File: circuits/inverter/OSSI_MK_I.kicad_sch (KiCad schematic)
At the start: 0 parts

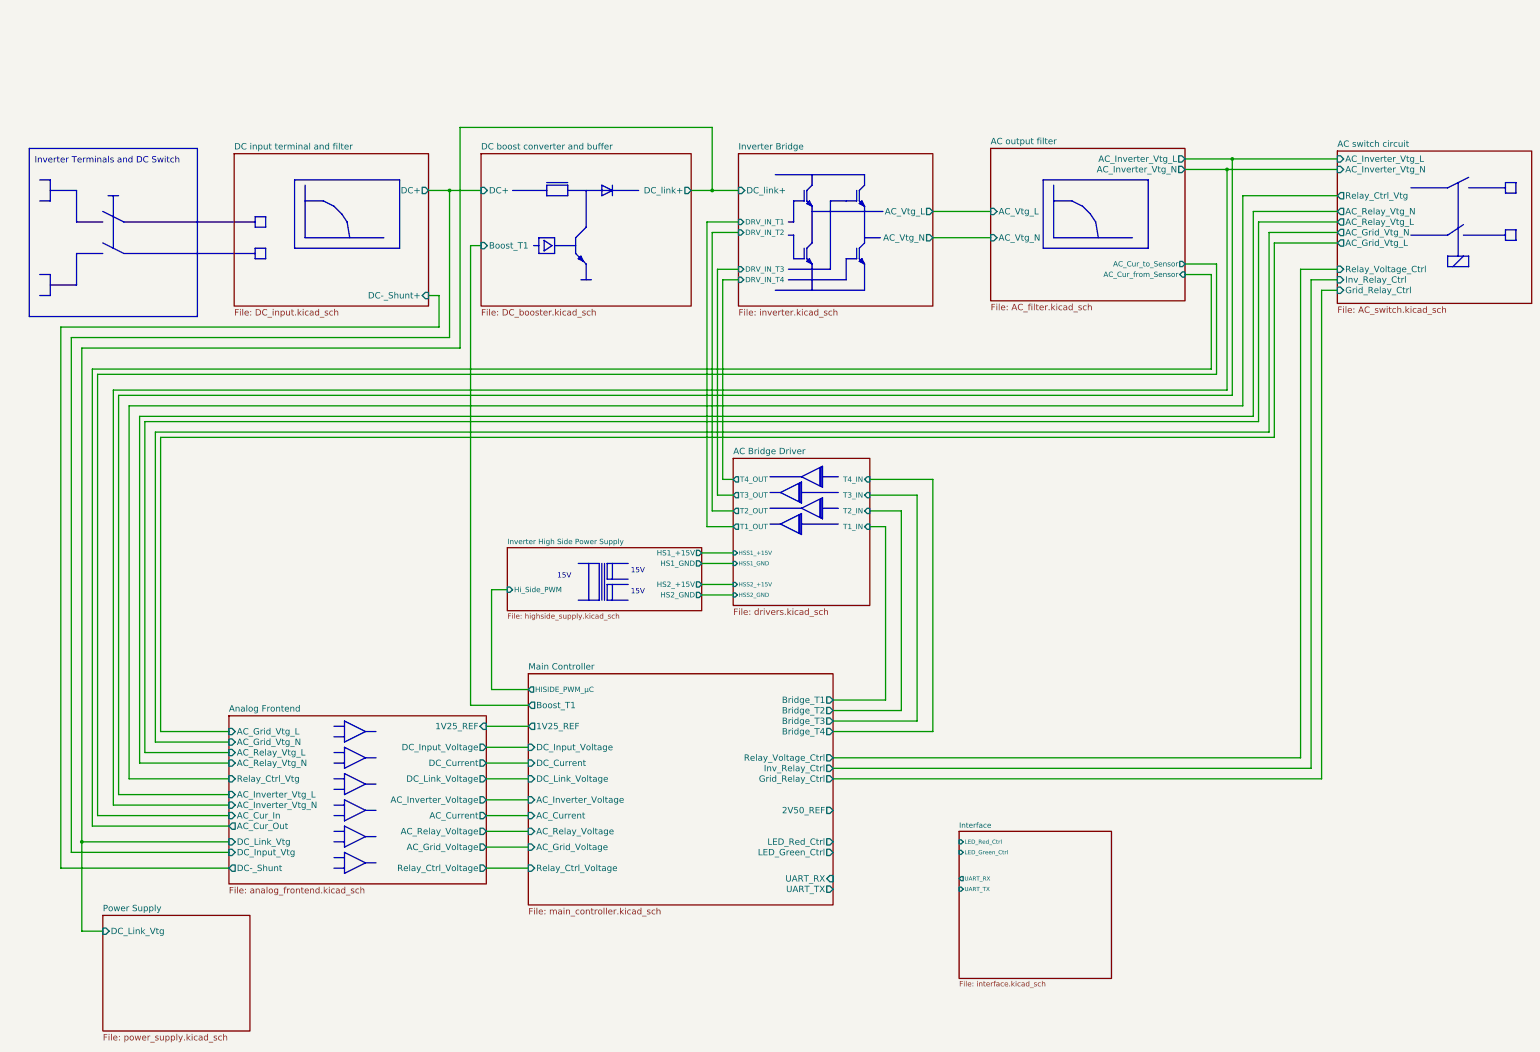
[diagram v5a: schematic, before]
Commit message: replaces controller schematics with Control Module 1
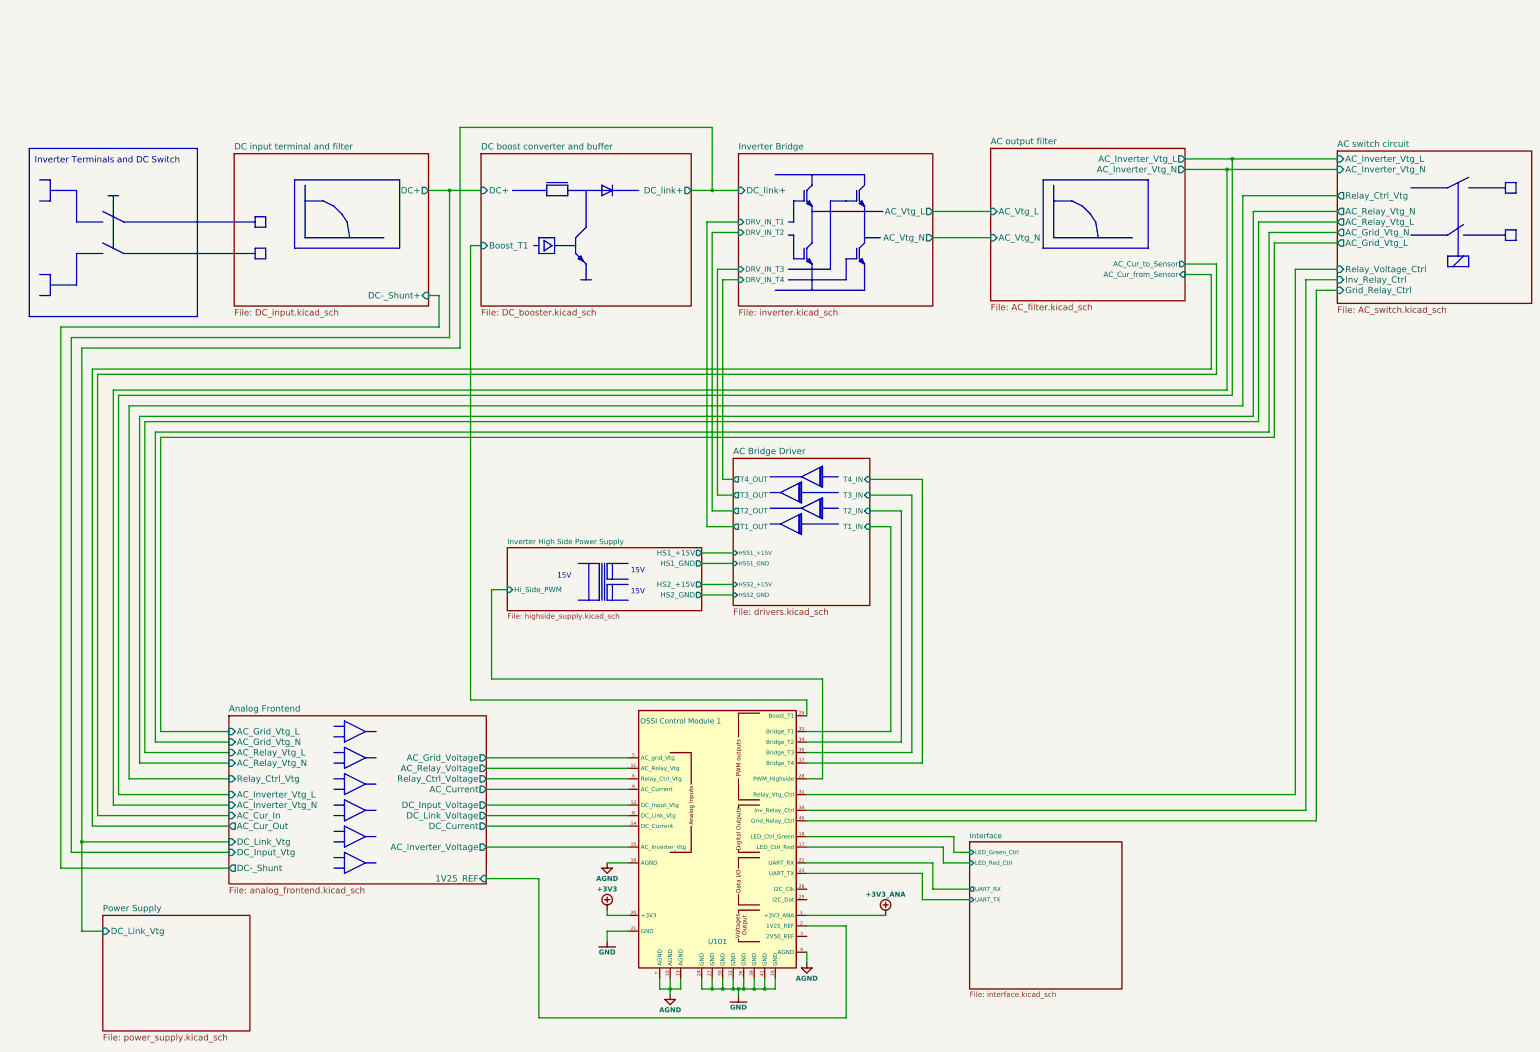
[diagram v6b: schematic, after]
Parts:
- added U101: OSSI Control Module 1, symbol OSSI_CM1:OSSI-CM1
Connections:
- net AC Bridge Driver /T1_IN: now also U101.32 (Bridge_T1)
- net AC Bridge Driver /T2_IN: now also U101.34 (Bridge_T2)
- net AC Bridge Driver /T3_IN: now also U101.35 (Bridge_T3)
- net AC Bridge Driver /T4_IN: now also U101.37 (Bridge_T4)
- net AC switch circuit/Grid_Relay_Ctrl: now also U101.40 (Grid_Relay_Ctrl)
- net AC switch circuit/Inv_Relay_Ctrl: now also U101.38 (Inv_Relay_Ctrl)
- net AC switch circuit/Relay_Voltage_Ctrl: now also U101.31 (Relay_Vtg_Ctrl)
- net Analog Frontend/1V25_REF: now also U101.2 (1V25_REF)
- net Analog Frontend/AC_Current: now also U101.9 (AC_Current)
- net Analog Frontend/AC_Grid_Voltage: now also U101.5 (AC_grid_Vtg)
- net Analog Frontend/AC_Inverter_Voltage: now also U101.15 (AC_Inverter_Vtg)
- net Analog Frontend/AC_Relay_Voltage: now also U101.11 (AC_Relay_Vtg)
- net Analog Frontend/DC_Current: now also U101.14 (DC_Current)
- net Analog Frontend/DC_Input_Voltage: now also U101.12 (DC_Input_Vtg)
- net Analog Frontend/DC_Link_Voltage: now also U101.8 (DC_Link_Vtg)
- net Analog Frontend/Relay_Ctrl_Voltage: now also U101.6 (Relay_Ctrl_Vtg)
- net DC boost converter and buffer/Boost_T1: now also U101.29 (Boost_T1)
- net Interface/LED_Green_Ctrl: now also U101.18 (LED_Ctrl_Green)
- net Interface/LED_Red_Ctrl: now also U101.17 (LED_Ctrl_Red)
- net Interface/UART_RX: now also U101.22 (UART_RX)
- net Interface/UART_TX: now also U101.23 (UART_TX)
- net Inverter High Side Power Supply/Hi_Side_PWM: now also U101.28 (PWM_Highside)
- new net +3V3: U101.1 (+3V3_ANA), U101.20 (+3V3)
- new net AGND: U101.10 (AGND), U101.13 (AGND), U101.16 (AGND), U101.4 (AGND), U101.7 (AGND)
- new net GND: U101.19 (GND), U101.21 (GND), U101.24 (GND), U101.27 (GND), U101.30 (GND), U101.33 (GND), U101.36 (GND), U101.39 (GND), U101.41 (GND)
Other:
- removed sheet Main Controller
